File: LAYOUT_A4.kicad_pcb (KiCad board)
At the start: 2 copper layers, 209.6 x 205.7 mm, 108 parts, among them SW1 DPST, SW10 DPST, SW11 DPST, SW12 DPST, SW13 DPST, SW14 DPST, SW15 DPST, SW16 DPST, SW2 DPST, SW3 DPST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

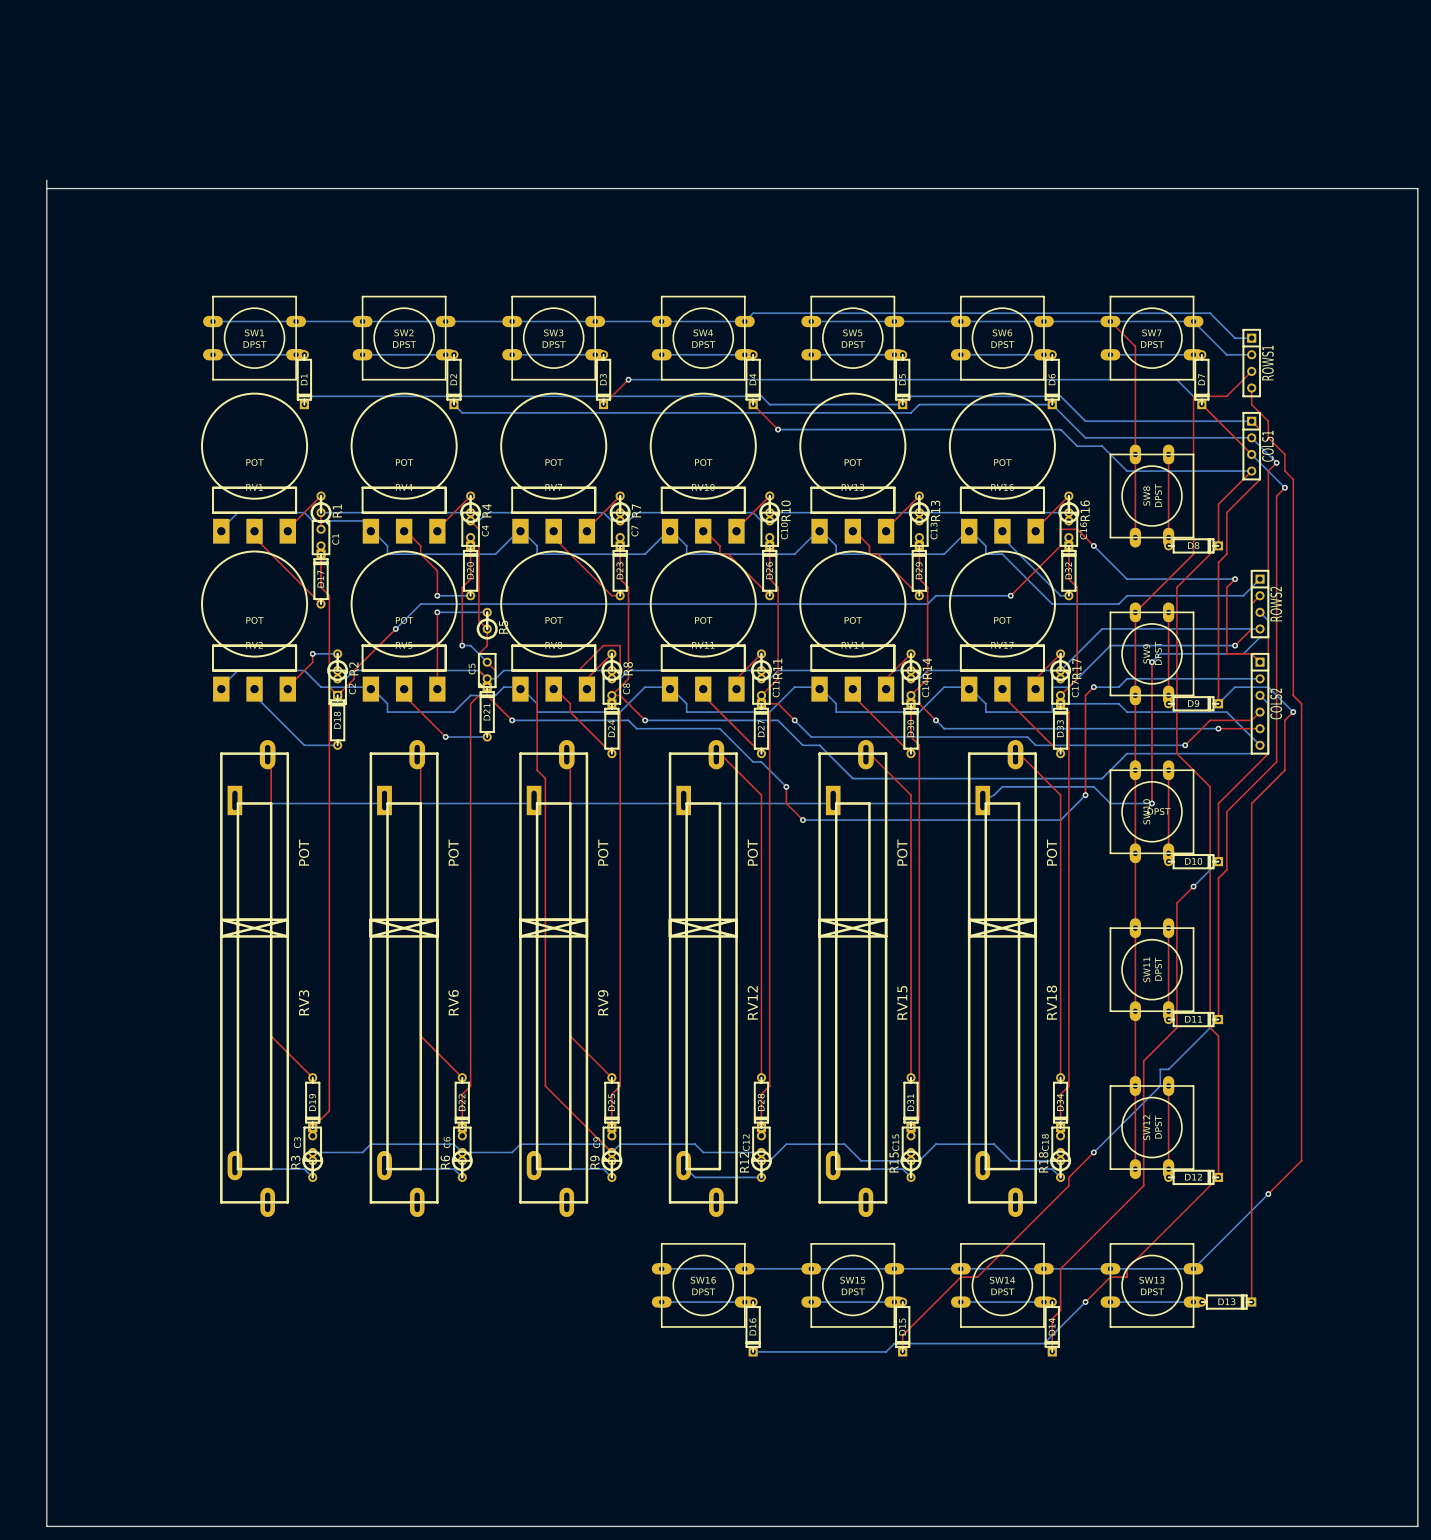
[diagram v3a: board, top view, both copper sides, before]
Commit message: MIDI ports added
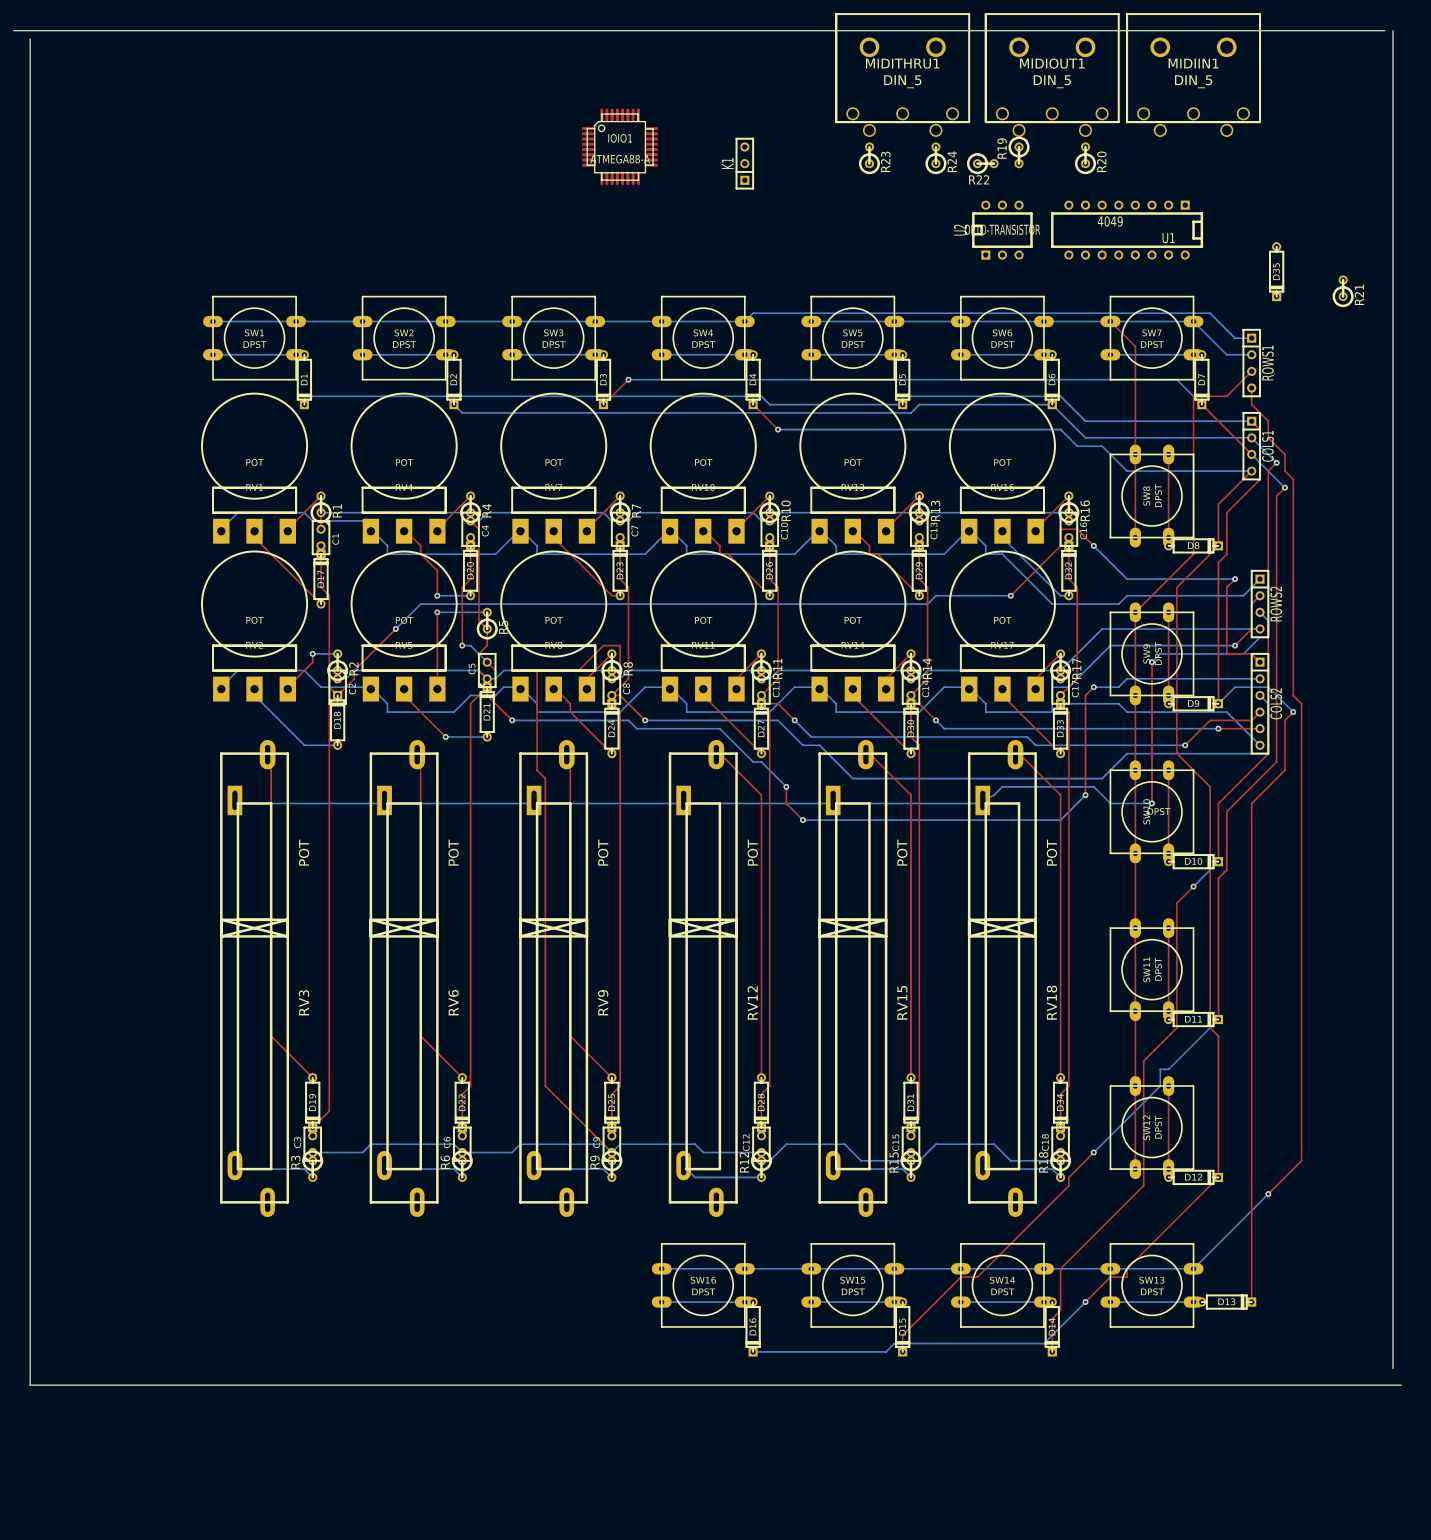
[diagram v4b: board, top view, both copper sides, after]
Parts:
- added D35: DIODE, D3, F.Cu at (180.3, 80.0)
- added IOIO1: ATMEGA88-A, TQFP32, F.Cu at (80.0, 61.0)
- added K1: CONN_3, SIL-3, F.Cu at (99.1, 63.5)
- added MIDIIN1: DIN_5, DIN_5, F.Cu at (167.6, 55.9)
- added MIDIOUT1: DIN_5, DIN_5, F.Cu at (146.1, 55.9)
- added MIDITHRU1: DIN_5, DIN_5, F.Cu at (123.2, 55.9)
- added R19: 220, R1, F.Cu at (141.0, 62.2)
- added R20: 220, R1, F.Cu at (151.1, 62.2)
- added R21: 220, R1, F.Cu at (190.5, 82.5)
- added R22: 280, R1, F.Cu at (135.9, 63.5)
- added R23: 220, R1, F.Cu at (118.1, 62.2)
- added R24: 220, R1, F.Cu at (128.3, 62.2)
- added U1: 4049, DIP-16__300, F.Cu at (157.5, 73.7)
- added U2: OPTO-TRANSISTOR, DIP-6__300, F.Cu at (138.4, 73.7)
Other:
- board size 209.6 x 205.7 mm -> 212.1 x 207 mm
